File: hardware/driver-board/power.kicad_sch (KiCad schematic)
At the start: 9 parts, among them SW1 SW_SPST, U5 LMR51430XDDCR

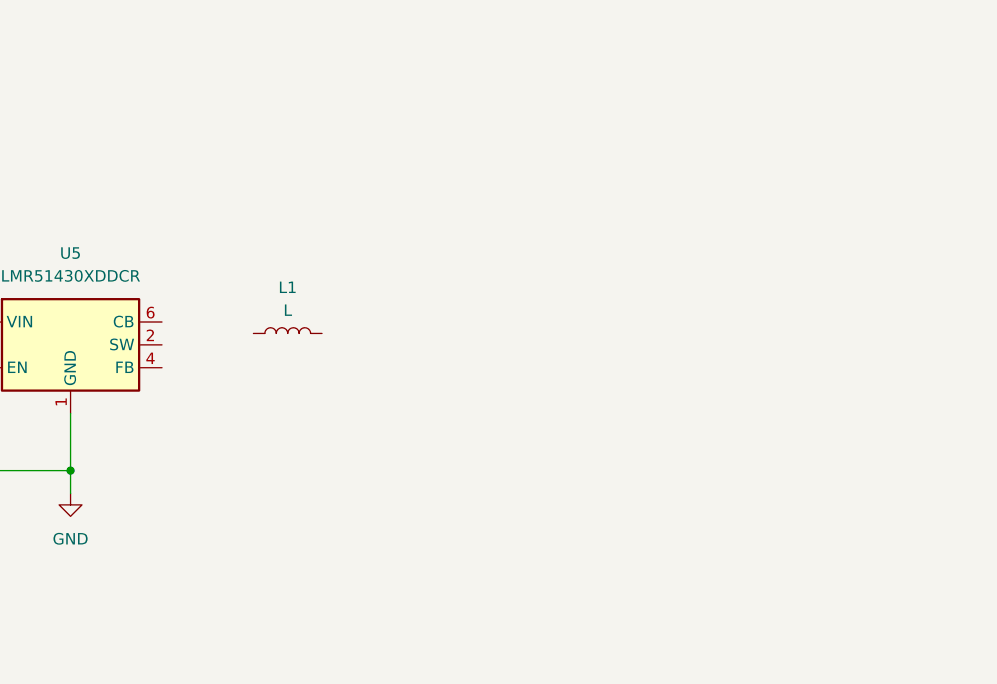
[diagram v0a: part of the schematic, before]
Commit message: Add buck regulator parts
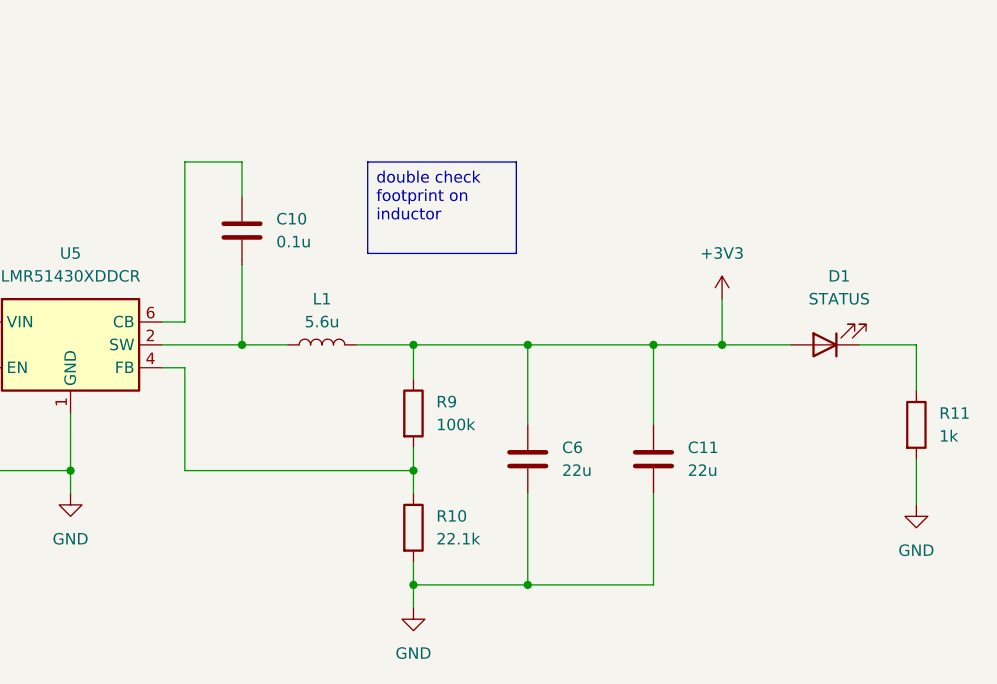
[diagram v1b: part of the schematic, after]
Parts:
- added C10: 0.1u, Capacitor_SMD:C_0603_1608Metric, symbol Device:C
- added C11, C6: 22u, Capacitor_SMD:C_1206_3216Metric, symbol Device:C
- added D1: STATUS, LED_SMD:LED_0603_1608Metric, symbol Device:LED
- added R10: 22.1k, Resistor_SMD:R_0603_1608Metric, symbol Device:R
- added R11: 1k, Resistor_SMD:R_0603_1608Metric, symbol Device:R
- added R9: 100k, Resistor_SMD:R_0603_1608Metric, symbol Device:R
- C5: footprint (none) -> Capacitor_SMD:C_0805_2012Metric
- L1: value L -> 5.6u; footprint (none) -> Inductor_SMD:L_Sunlord_SWPA6045S; JLCPCB (none) -> C96960
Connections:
- net GND: now also C11.2, C6.2, R10.2, R11.2
- net at L1.1: now also U5.2 (SW), C10.2
- net +3V3: now reaches L1.2
- net +3V3: now also C11.1, C6.1, D1.2 (A), R9.1
- net at U5.4 (FB): now also R10.1, R9.2
- net at U5.6 (CB): now also C10.1
- new net: D1.1 (K), R11.1
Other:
- moved on the sheet: L1

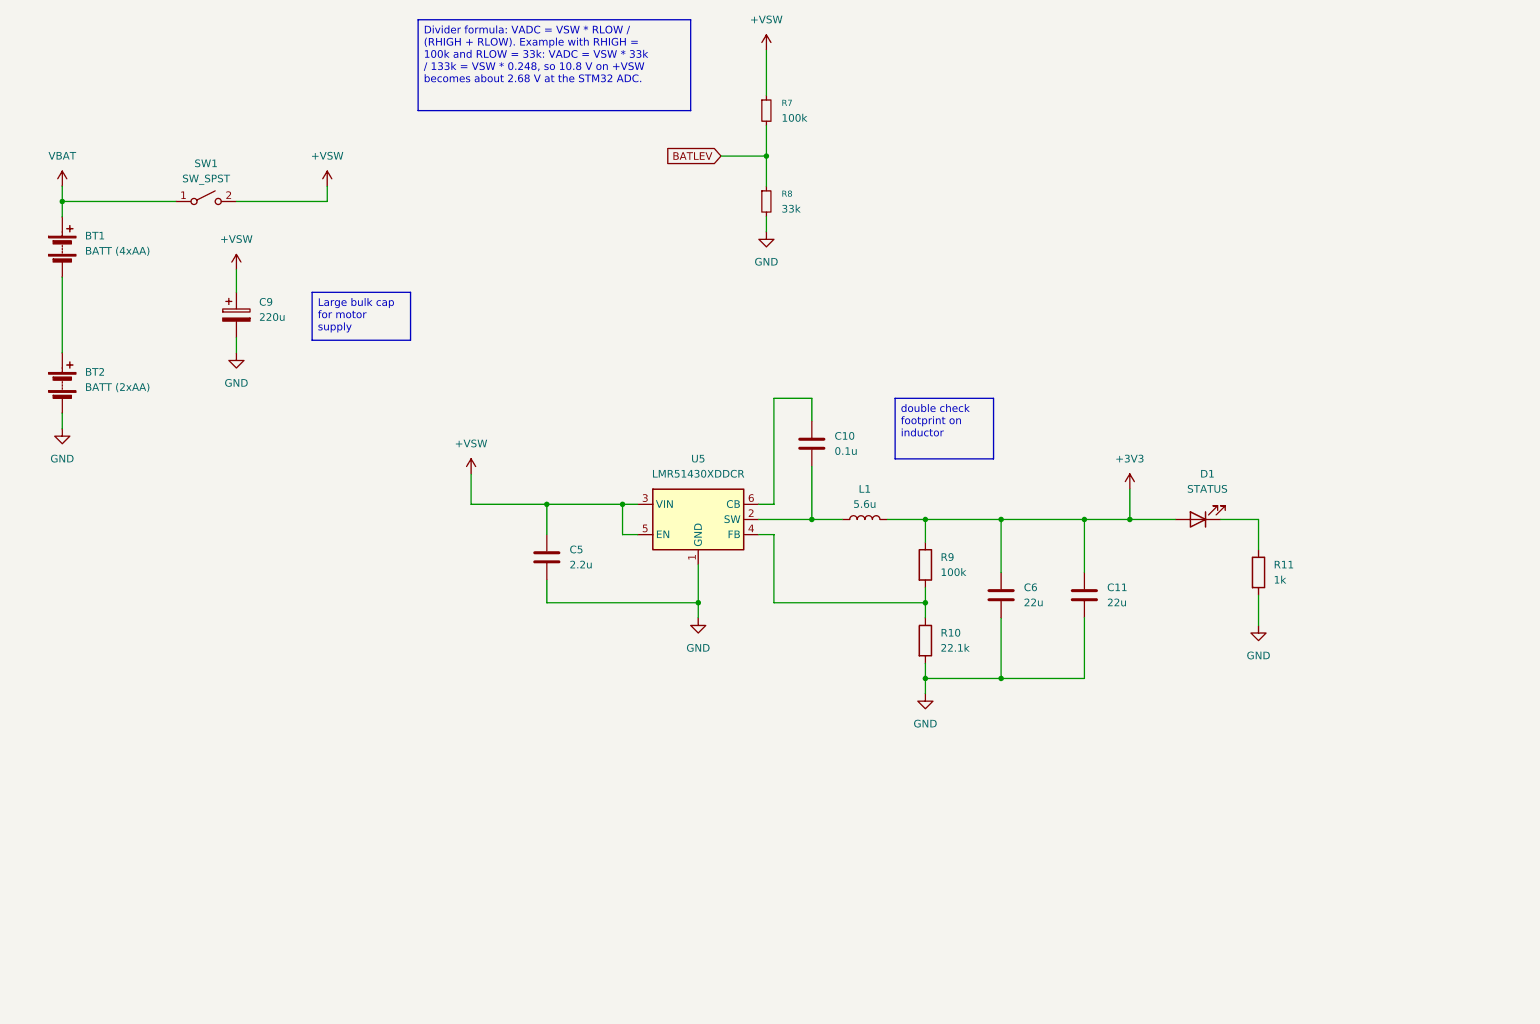
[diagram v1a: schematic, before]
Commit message: Checkpoint driver board schematic
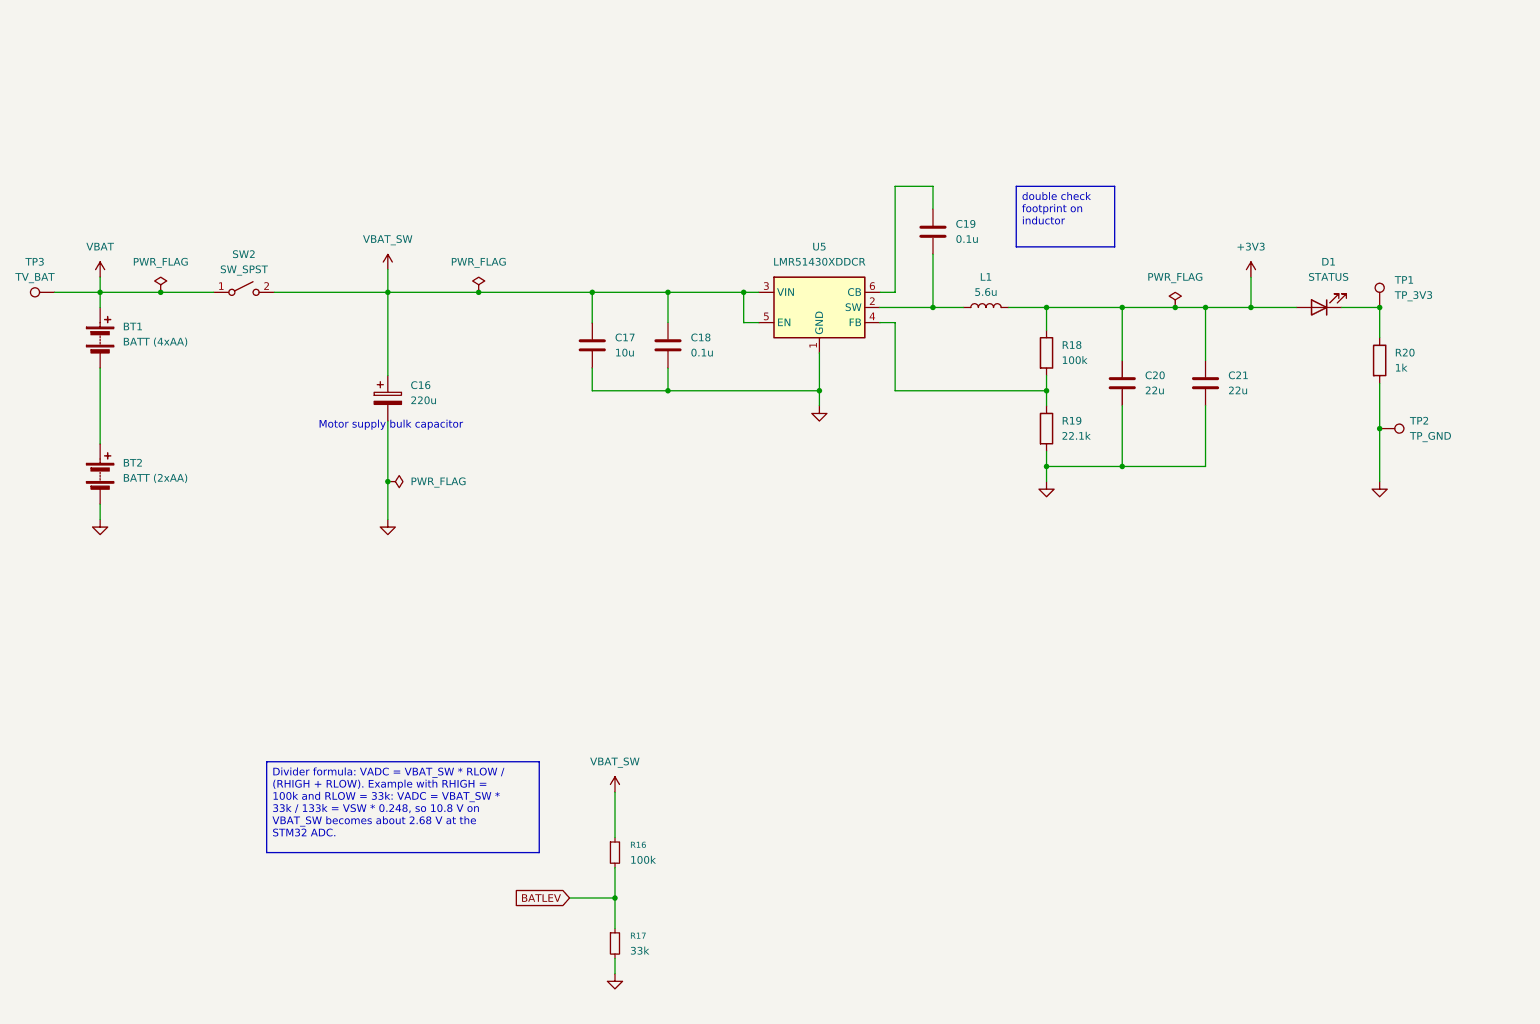
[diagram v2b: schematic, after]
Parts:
- added C17: 10u, Capacitor_SMD:C_0805_2012Metric, symbol Device:C
- added TP1: TP_3V3, symbol Connector:TestPoint
- added TP2: TP_GND, symbol Connector:TestPoint
- added TP3: TV_BAT, symbol Connector:TestPoint
- C18: renamed from C5; value 2.2u -> 0.1u; footprint Capacitor_SMD:C_0805_2012Metric -> Capacitor_SMD:C_0402_1005Metric
- renumbered C9 to C16, C10 to C19, C6 to C20, C11 to C21, R7 to R16, R8 to R17, R9 to R18, R10 to R19, R11 to R20, SW1 to SW2
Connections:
- net GND: now also C17.2, TP2.1
- net VBAT: now also TP3.1
- net at D1.1 (K), R20.1: now also TP1.1
- net +VSW renamed VBAT_SW
- net VBAT_SW: now also C17.1
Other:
- note added: "Motor supply bulk capacitor"
- moved on the sheet: BT1, BT2, C16, C18, C19, C20, C21, D1, L1, R16, R17, R18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

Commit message: Wrap up Rev A schematic pre-layout tasks
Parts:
- added F1: PTC_2.6A_16V, Fuse:Fuse_1812_4532Metric, symbol Device:Polyfuse
- C17: footprint Capacitor_SMD:C_0805_2012Metric -> Capacitor_SMD:C_1206_3216Metric; JLCPCB (none) -> C13585; JLCPCB Type (none) -> Basic
- C18: footprint Capacitor_SMD:C_0402_1005Metric -> Capacitor_SMD:C_0603_1608Metric; JLCPCB (none) -> C14663; JLCPCB Type (none) -> Basic
- C19: JLCPCB (none) -> C14663; JLCPCB Type (none) -> Basic
- C20, C21: JLCPCB (none) -> C12891; JLCPCB Type (none) -> Basic
- D1: JLCPCB (none) -> C12624; JLCPCB Type (none) -> Basic
- R16: footprint (none) -> Resistor_SMD:R_0603_1608Metric; JLCPCB (none) -> C25803; JLCPCB Type (none) -> Basic
- R17: footprint (none) -> Resistor_SMD:R_0603_1608Metric; JLCPCB (none) -> C4216; JLCPCB Type (none) -> Basic
- R18: JLCPCB Type (none) -> Basic
- R20: JLCPCB (none) -> C21190; JLCPCB Type (none) -> Basic
- TP1, TP2, TP3: footprint (none) -> TestPoint:TestPoint_Pad_2.0x2.0mm
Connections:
- net +3V3: now also TP1.1
- net VBAT: now also F1.1; no longer SW2.1 (A)
- net at D1.1 (K), R20.1: no longer TP1.1
- new net: F1.2, SW2.1 (A)
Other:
- moved on the sheet: BT1, C16, D1, R20, SW2, TP1, TP2

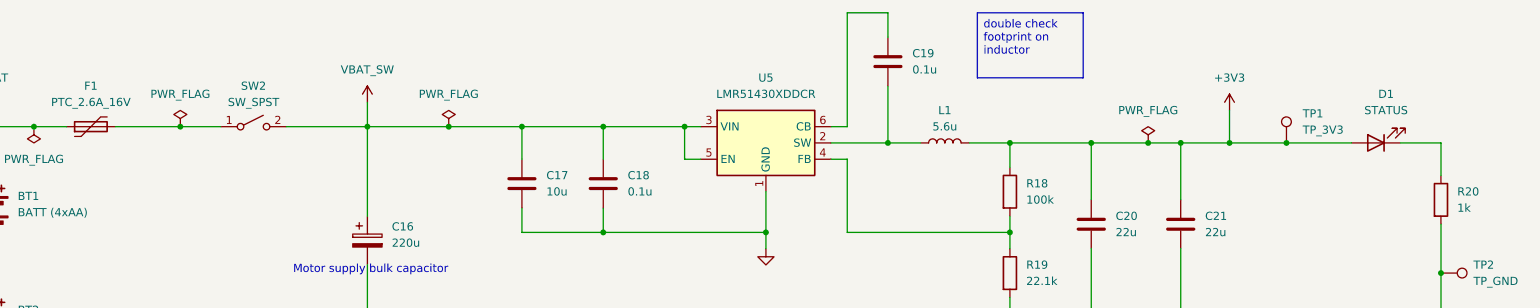
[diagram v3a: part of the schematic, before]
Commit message: Add custom power entry footprints
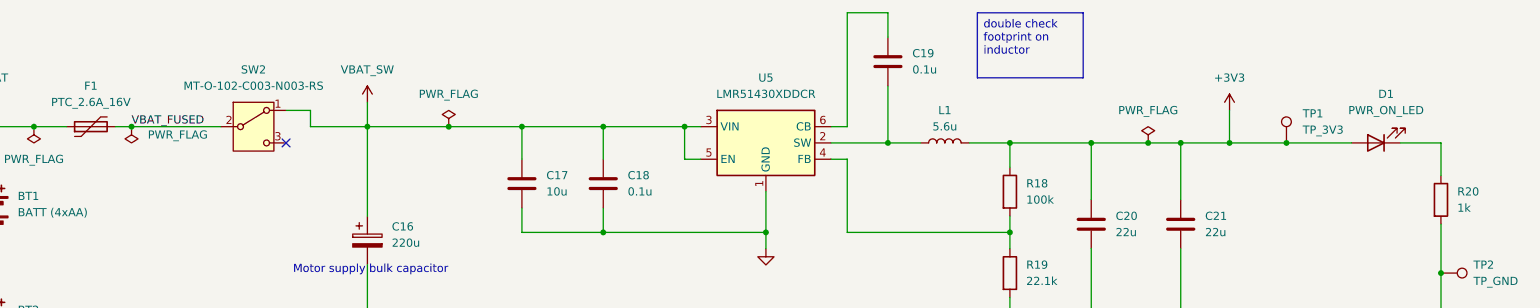
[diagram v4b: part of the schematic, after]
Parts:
- removed SW2: SW_SPST, symbol Switch:SW_SPST
- added SW2: MT-O-102-C003-N003-RS, CustomParts:SW_SPDT_Angled_YuenFung_MT-O-102-C003-N003-RS, symbol Switch:SW_SPDT
- BT1, BT2: footprint (none) -> CustomParts:Romi_Chassis_BatteryContactPair_2Slot_10_44mm_FirstPass
- D1: value STATUS -> PWR_ON_LED; JLCPCB C12624 -> C2286
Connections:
- net VBAT_SW: now also SW2.1 (A)
- net VBAT_FUSED: now reaches F1.2
- net VBAT_FUSED: now also SW2.2 (B)
- no-connect marks 0 -> 1
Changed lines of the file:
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@@
 	)
 	(junction
+		(at 97.79 66.04)
+		(diameter 0)
+		(color 0 0 0 0)
+	)
+	(junction
 		(at 232.41 68.58)
 		(diameter 0)
@@
 	)
 	(junction
-		(at 179.07 68.58)
+		(at 110.49 66.04)
 		(diameter 0)
 		(color 0 0 0 0)
 	)
 	(junction
-		(at 45.72 66.04)
+		(at 179.07 68.58)
 		(diameter 0)
 		(color 0 0 0 0)
 	)
 	(junction
-		(at 110.49 66.04)
+		(at 45.72 66.04)
 		(diameter 0)
 		(color 0 0 0 0)
@@
 	)
 	(junction
-		(at 68.58 66.04)
-		(diameter 0)
-		(color 0 0 0 0)
-	)
-	(junction
 		(at 121.92 66.04)
 		(diameter 0)
@@
 	)
 	(junction
-		(at 97.79 66.04)
+		(at 198.12 95.25)
 		(diameter 0)
 		(color 0 0 0 0)
 	)
 	(junction
-		(at 198.12 95.25)
+		(at 198.12 82.55)
 		(diameter 0)
 		(color 0 0 0 0)
 	)
 	(junction
-		(at 198.12 82.55)
+		(at 39.37 66.04)
 		(diameter 0)
 		(color 0 0 0 0)
 	)
 	(junction
-		(at 39.37 66.04)
+		(at 60.96 66.04)
 		(diameter 0)
 		(color 0 0 0 0)
 	)
+	(no_connect
+		(at 85.09 68.58)
+	)
 	(wire
 		(pts
-			(xy 160.02 82.55) (xy 160.02 85.09)
+			(xy 88.9 63.5) (xy 88.9 66.04)
 		)
 		(stroke
@@
 	(wire
 		(pts
-			(xy 97.79 66.04) (xy 97.79 80.01)
+			(xy 160.02 82.55) (xy 160.02 85.09)
 		)
 		(stroke
@@
 	(wire
 		(pts
+			(xy 88.9 66.04) (xy 97.79 66.04)
+		)
+		(stroke
+			(width 0)
+			(type default)
+		)
+	)
+	(wire
+		(pts
 			(xy 170.18 68.58) (xy 179.07 68.58)
 		)
@@
 	(wire
 		(pts
-			(xy 68.58 66.04) (xy 74.93 66.04)
-		)
-		(stroke
-			(width 0)
-			(type default)
-		)
-	)
-	(wire
-		(pts
 			(xy 232.41 68.58) (xy 232.41 63.5)
 		)
@@
 	(wire
 		(pts
-			(xy 85.09 66.04) (xy 110.49 66.04)
+			(xy 97.79 66.04) (xy 110.49 66.04)
 		)
 		(stroke
@@
 	(wire
 		(pts
-			(xy 58.42 66.04) (xy 68.58 66.04)
+			(xy 58.42 66.04) (xy 60.96 66.04)
 		)
 		(stroke
@@
 	(wire
 		(pts
+			(xy 85.09 63.5) (xy 88.9 63.5)
+		)
+		(stroke
+			(width 0)
+			(type default)
+		)
+	)
+	(wire
+		(pts
+			(xy 60.96 66.04) (xy 74.93 66.04)
+		)
+		(stroke
+			(width 0)
+			(type default)
+		)
+	)
+	(wire
+		(pts
 			(xy 259.08 68.58) (xy 265.43 68.58)
 		)
@@
 	(wire
 		(pts
+			(xy 97.79 66.04) (xy 97.79 80.01)
+		)
+		(stroke
+			(width 0)
+			(type default)
+		)
+	)
+	(wire
+		(pts
 			(xy 134.62 66.04) (xy 147.32 66.04)
 		)
@@
 		)
 	)
+	(label "VBAT_FUSED"
+		(at 60.96 66.04 0)
+		(effects
+			(font
+				(size 1.27 1.27)
+			)
+			(justify left bottom)
+		)
+	)
 	(global_label "BATLEV"
 		(shape input)
@@
 			)
 		)
-		(property "Footprint" ""
+		(property "Footprint" "CustomParts:Romi_Chassis_BatteryContactPair_2Slot_10_44mm_FirstPass"
 			(at 39.37 77.216 90)
 			(hide yes)
@@
 			)
 		)
-		(property "Datasheet" ""
+		(property "Datasheet" "https://www.pololu.com/file/0J1201/power-distribution-board-for-romi-chassis-dimension-diagram.pdf"
 			(at 39.37 77.216 90)
 			(hide yes)
@@
 			)
 		)
-		(property "KLC_S3.3" ""
-			(at 39.37 78.74 0)
-			(hide yes)
-			(show_name no)
-			(do_not_autoplace no)
-			(effects
-				(font
-					(size 1.27 1.27)
-				)
-			)
-		)
-		(property "KLC_S4.1" ""
-			(at 39.37 78.74 0)
-			(hide yes)
-			(show_name no)
-			(do_not_autoplace no)
-			(effects
-				(font
-					(size 1.27 1.27)
-				)
-			)
-		)
 		(pin "1"
 		)
@@
 			)
 		)
-		(property "Footprint" ""
+		(property "Footprint" "CustomParts:Romi_Chassis_BatteryContactPair_2Slot_10_44mm_FirstPass"
 			(at 39.37 94.996 90)
 			(hide yes)
@@
 			)
 		)
-		(property "Datasheet" ""
+		(property "Datasheet" "https://www.pololu.com/file/0J1201/power-distribution-board-for-romi-chassis-dimension-diagram.pdf"
 			(at 39.37 94.996 90)
 			(hide yes)
@@
 			)
 		)
-		(property "Value" "STATUS"
+		(property "Value" "PWR_ON_LED"
 			(at 256.8575 63.5 0)
 			(show_name no)
@@
 			)
 		)
-		(property "JLCPCB" "C12624"
+		(property "JLCPCB" "C2286"
 			(at 255.27 68.58 0)
 			(hide yes)
@@
 	)
 	(symbol
-		(lib_id "Switch:SW_SPST")
+		(lib_id "Switch:SW_SPDT")
 		(at 80.01 66.04 0)
 		(unit 1)
@@
 		(fields_autoplaced yes)
 		(property "Reference" "SW2"
+			(at 80.01 57.15 0)
+			(show_name no)
+			(do_not_autoplace no)
+			(effects
+				(font
+					(size 1.27 1.27)
+				)
+			)
+		)
+		(property "Value" "MT-O-102-C003-N003-RS"
 			(at 80.01 59.69 0)
 			(show_name no)
@@
 			)
 		)
-		(property "Value" "SW_SPST"
-			(at 80.01 62.23 0)
+		(property "Footprint" "CustomParts:SW_SPDT_Angled_YuenFung_MT-O-102-C003-N003-RS"
+			(at 80.01 66.04 0)
+			(hide yes)
 			(show_name no)
 			(do_not_autoplace no)
@@
 			)
 		)
-		(property "Footprint" ""
+		(property "Datasheet" "${KIPRJMOD}/datasheets/C1788495.pdf"
+			(at 80.01 73.66 0)
+			(hide yes)
+			(show_name no)
+			(do_not_autoplace no)
+			(effects
+				(font
+					(size 1.27 1.27)
+				)
+			)
+		)
+		(property "Description" "Switch, single pole double throw - MT-O-102-C003-N003-RS"
 			(at 80.01 66.04 0)
 			(hide yes)
@@
 			)
 		)
-		(property "Datasheet" ""
+		(property "JLCPCB" "C1788495"
 			(at 80.01 66.04 0)
 			(hide yes)
@@
 			)
 		)
-		(property "Description" "Single Pole Single Throw (SPST) switch"
+		(property "MPN" "MT-O-102-C003-N003-RS"
 			(at 80.01 66.04 0)
 			(hide yes)
@@
 			)
 		)
-		(property "KLC_S3.3" ""
+		(property "Manufacturer" "YUE FUNG"
 			(at 80.01 66.04 0)
 			(hide yes)
@@
 			)
 		)
-		(property "KLC_S4.1" ""
+		(property "JLCPCB Type" "Extended"
 			(at 80.01 66.04 0)
 			(hide yes)
@@
 			)
 		)
+		(pin "2"
+		)
 		(pin "1"
 		)
-		(pin "2"
+		(pin "3"
 		)
 		(instances
@@
 	(symbol
 		(lib_id "PCM_4ms_Power-symbol:PWR_FLAG")
-		(at 68.58 66.04 0)
+		(at 60.96 66.04 180)
 		(unit 1)
 		(body_style 1)
@@
 		(fields_autoplaced yes)
 		(property "Reference" "#FLG02"
-			(at 68.58 64.135 0)
+			(at 60.96 67.945 0)
 			(hide yes)
 			(show_name no)
@@
 		)
 		(property "Value" "PWR_FLAG"
-			(at 68.58 60.96 0)
+			(at 63.5 67.3099 0)
 			(show_name no)
 			(do_not_autoplace no)
@@
 					(size 1.27 1.27)
 				)
+				(justify right)
 			)
 		)
 		(property "Footprint" ""
-			(at 68.58 66.04 0)
+			(at 60.96 66.04 0)
 			(hide yes)
 			(show_name no)
@@
 		)
 		(property "Datasheet" ""
-			(at 68.58 66.04 0)
+			(at 60.96 66.04 0)
 			(hide yes)
 			(show_name no)
@@
 		)
 		(property "Description" ""
-			(at 68.58 66.04 0)
+			(at 60.96 66.04 0)
 			(hide yes)
 			(show_name no)
